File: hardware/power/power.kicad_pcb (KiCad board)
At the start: 2 copper layers, 100 x 60 mm, 82 parts, among them J1 PD 20V IN, J2 POWER SWITCH, J3 BRAIN, J4 CELLS, Q1 AO3400A, Q2 AO3400A, Q3 AO3400A, Q4 AO3400A, Q5 AO3400A, Q6 AO3400A, SW1 WAKE, U1 BQ24610, U2 BQ76920, U3 INA219

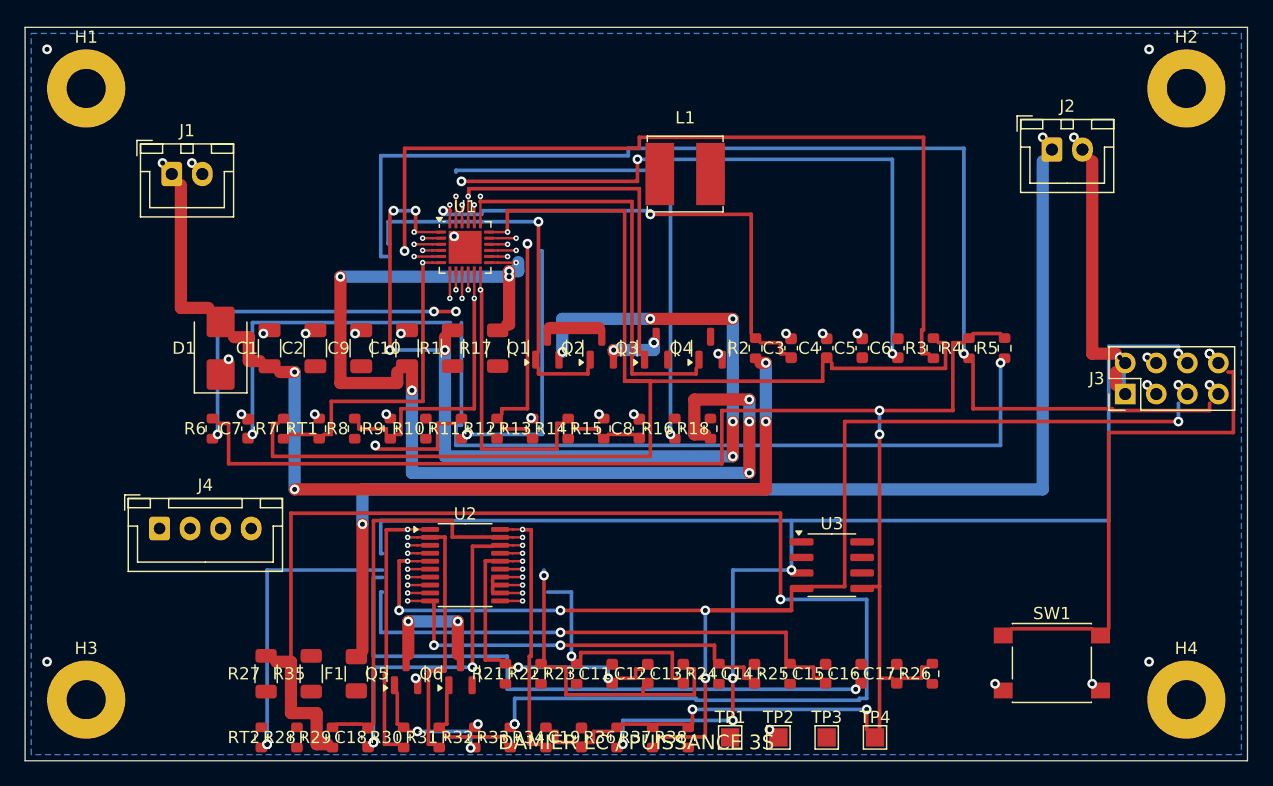
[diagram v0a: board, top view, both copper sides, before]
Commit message: Bobines : vias d'empilement hors des spires ; puissance et horloge régénérées
Les trois vias d'empilement de chaque bobine du quadrant tombaient dans
les bandes de spires des deux autres couches et court-circuitaient la
bobine ; elles sont décalées radialement hors des bandes, reliées par
un tronçon radial, le net tie posé sur le tronçon de la dernière
jonction dans le creux, et les contrôles maison n'exemptent plus que
les deux pastilles du net tie.

Carte puissance et horloge régénérées avec les générateurs corrigés
(DRC KiCad réduit aux nets ouverts et à la sérigraphie), tableaux et
notes mis à jour, rapports de DRC ignorés par git.
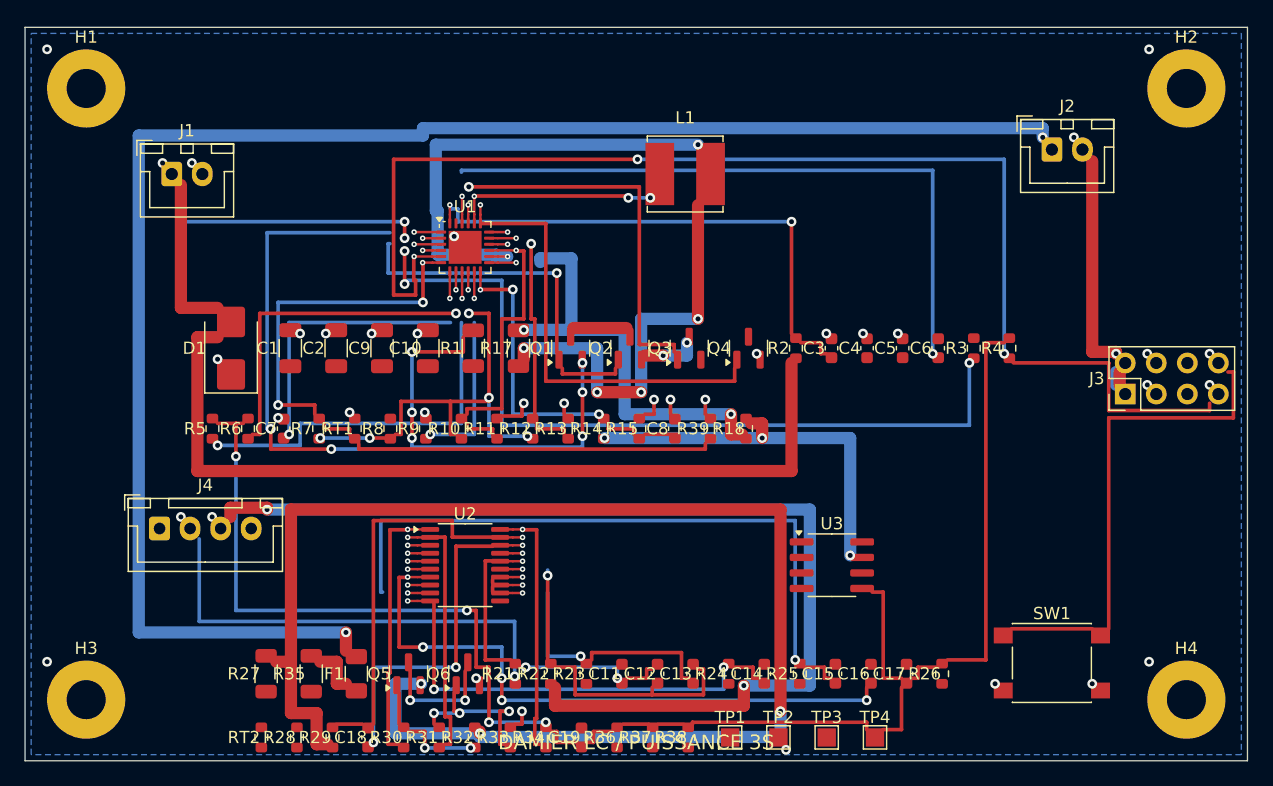
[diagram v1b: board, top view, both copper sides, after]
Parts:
- removed R16: 0R, Resistor_SMD:R_0603_1608Metric
- added R39: 30k1, Resistor_SMD:R_0603_1608Metric, F.Cu at (56.1, 32.8)
- Q1, Q2: value AO3400A -> AO3401A
- R11: value 10k -> 3k16
- R13: value 50k -> 17k8
- R17: value 10m -> 50m
- R7: value 10k -> 5k23
- R9: value 50k -> 43k2
- moved R5 65.1 mm to (15.3, 32.8)
- moved C5 3.30 mm to (71.8, 26.2)
- moved R2 3.30 mm to (63.1, 26.2)
- moved C3 3.30 mm to (66.0, 26.2)
- moved C4 3.30 mm to (68.9, 26.2)
- moved C6 3.30 mm to (74.7, 26.2)
- moved R3 3.30 mm to (77.6, 26.2)
- moved R4 3.30 mm to (80.5, 26.2)
- moved Q4 3.10 mm to (59.2, 26.2)
- moved R10 2.91 mm to (35.7, 32.8)
- moved R12 2.91 mm to (41.5, 32.8)
- moved R14 2.91 mm to (47.3, 32.8)
- moved C7 2.91 mm to (21.1, 32.8)
- moved R7 2.91 mm to (24.1, 32.8)
- moved R8 2.91 mm to (29.9, 32.8)
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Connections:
- Q5 pad 2: GND -> PACK-PRE
- Q6 pad 2: PACK-PRE -> GND
- R32 pad 2: GND -> PACK-PRE
- R33 pad 2: PACK-PRE -> GND
- R7 pad 1: TS -> VREF
- R7 pad 2: REGN -> TS
- U1 pad 23: BATDRV -> (no net)
- U2 pad 11: AFE_NC -> (no net)
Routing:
- net SDA: track 116.9 -> 1.84 mm, vias 6 -> 1
- net SCL: track 107.1 -> 1.84 mm, vias 7 -> 1
- net REGN: track 99.3 -> 1.51 mm
- net CELL2: track 0.00 -> 86.7 mm, vias 0 -> 3
- net SRP: track 1.51 -> 72.0 mm, vias 1 -> 6
- net SRN: track 86.8 -> 37.3 mm, vias 8 -> 3
- net BATDRV: track 41.5 -> 0.00 mm, vias 2 -> 0
- net VBAT_OUT: track 95.7 -> 134.4 mm
- net CELL1: track 0.00 -> 37.3 mm, vias 0 -> 2
- net PACK+: track 0.00 -> 35.7 mm, vias 0 -> 3
- net TS: track 25.8 -> 61.1 mm, vias 1 -> 3
- net VREF: track 1.51 -> 35.9 mm, vias 1 -> 6
- net CHG_STAT2: track 64.0 -> 32.4 mm
- net VAD: track 78.0 -> 107.3 mm, vias 6 -> 4
- net TS1: track 25.5 -> 1.84 mm, vias 3 -> 1
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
